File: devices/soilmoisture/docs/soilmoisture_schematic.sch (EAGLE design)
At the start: 31 parts, among them Q1 SSM6P15FU, Q2 SSM6P15FU, Q3 2SK2009, Q4 2SK2009, SW1 OTA_BTN, U1 nRF52832, U2 RFM95C-915, U3 FM25V02-8KB, U4 MCP1700-2502E, U5 W25Q16-2MB

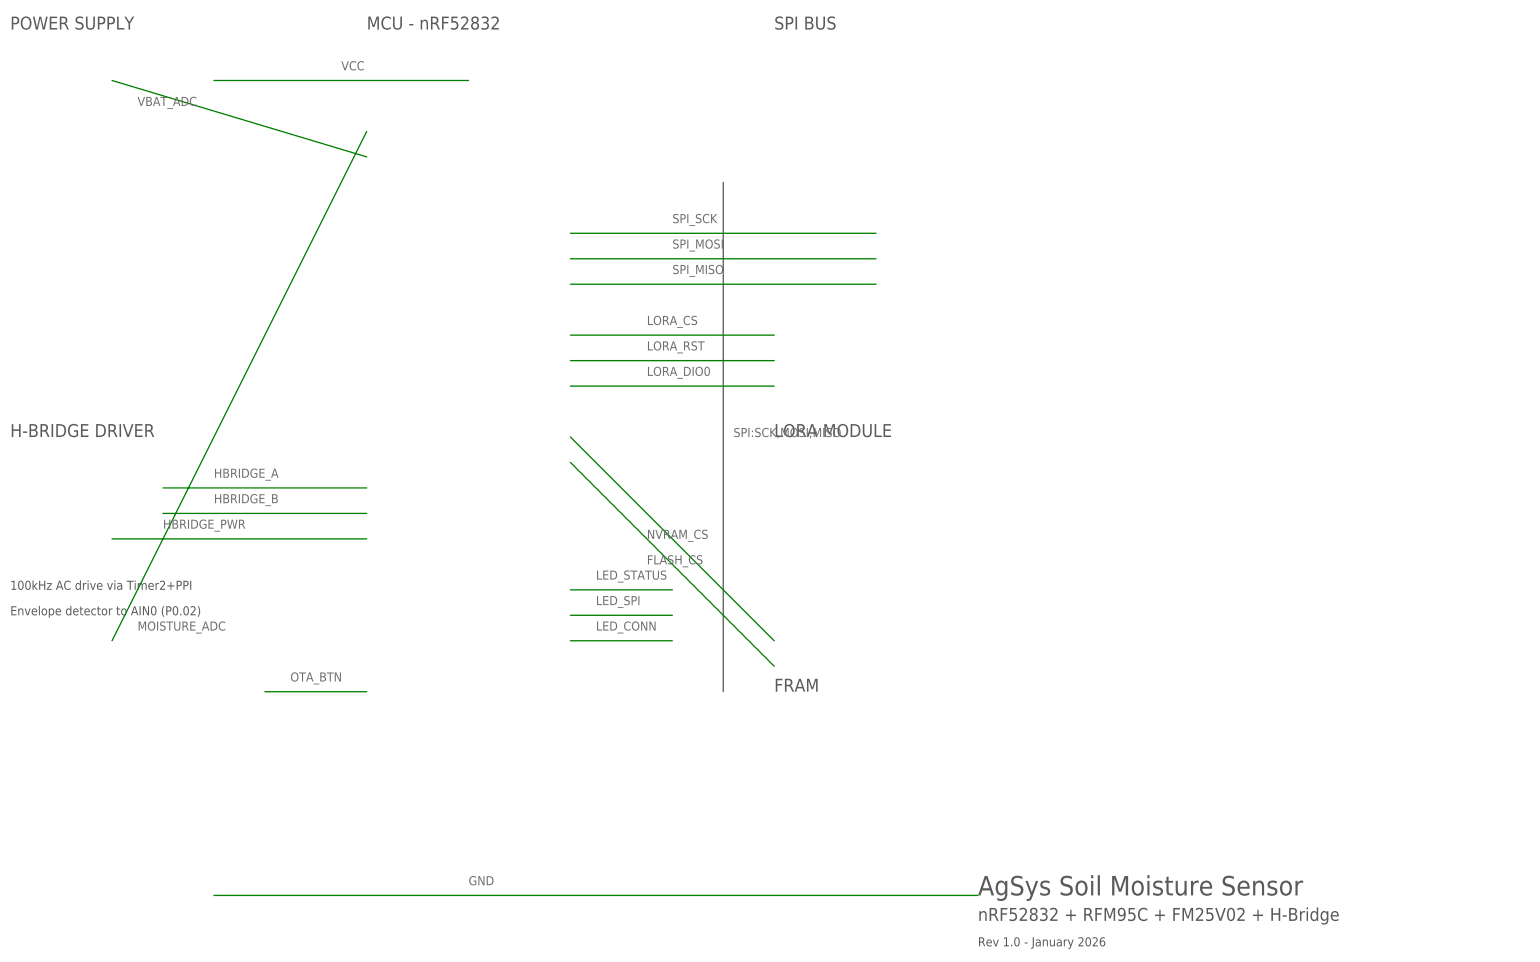
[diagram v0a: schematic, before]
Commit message: Initial commit - the soil moisture controller based on the amazing Nordic Semiconductor vRF52832 micro controller
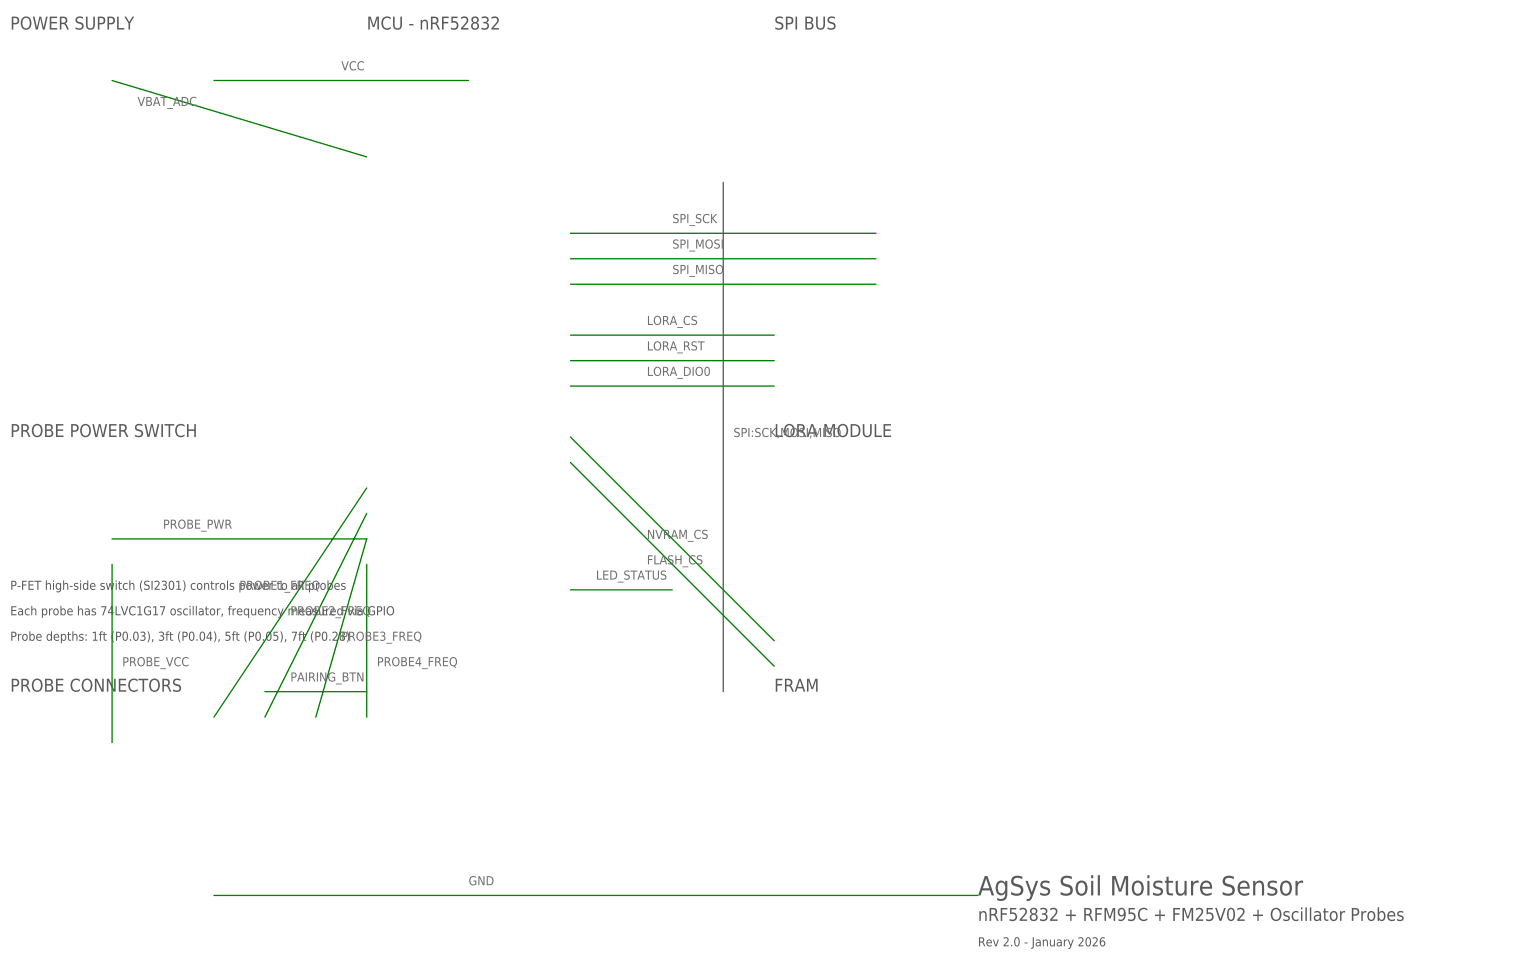
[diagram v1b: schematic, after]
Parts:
- removed D1, D2: BAT54S, diode:BAT54S
- removed LED2: YELLOW, led:LED
- removed LED3: BLUE, led:LED
- removed PROBE1: CAP_PROBE, connector:PROBE
- removed Q2: SSM6P15FU, mosfet:SSM6P15FU
- removed Q3, Q4: 2SK2009, mosfet:2SK2009
- added J1: PROBE1-1FT, connector:CONN_3
- added J2: PROBE2-3FT, connector:CONN_3
- added J3: PROBE3-5FT, connector:CONN_3
- added J4: PROBE4-7FT, connector:CONN_3
- added R7: 10K, resistor:R
- Q1: value SSM6P15FU -> SI2301-PFET; device mosfet:SSM6P15FU -> mosfet:SI2301
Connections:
- net OTA_BTN renamed PAIRING_BTN
- removed net HBRIDGE_A: Q1.G, Q3.G, U1.P0.14
- removed net HBRIDGE_B: Q2.G, Q4.G, U1.P0.15
- removed net HBRIDGE_PWR: U1.P0.16
- removed net LED_CONN: LED3.A, U1.P0.20
- removed net LED_SPI: LED2.A, U1.P0.19
- removed net MOISTURE_ADC: U1.P0.02/AIN0
- new net PROBE1_FREQ: J1.3, U1.P0.03
- new net PROBE2_FREQ: J2.3, U1.P0.04
- new net PROBE3_FREQ: J3.3, U1.P0.05
- new net PROBE4_FREQ: J4.3, U1.P0.28
- new net PROBE_PWR: Q1.G, R7.1, U1.P0.16
- new net PROBE_VCC: J1.1, J2.1, J3.1, J4.1, Q1.S
- net LED_STATUS: now also R3.1
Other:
- note added: "Each probe has 74LVC1G17 oscillator, frequency measured via GPIO"
- note added: "P-FET high-side switch (SI2301) controls power to all probes"
- note added: "PROBE CONNECTORS"
- note added: "PROBE POWER SWITCH"
- note added: "Probe depths: 1ft (P0.03), 3ft (P0.04), 5ft (P0.05), 7ft (P0.28)"
- note added: "Rev 2.0 - January 2026"
- note added: "nRF52832 + RFM95C + FM25V02 + Oscillator Probes"
- note removed: "100kHz AC drive via Timer2+PPI"
- note removed: "Envelope detector to AIN0 (P0.02)"
- note removed: "H-BRIDGE DRIVER"
- note removed: "Rev 1.0 - January 2026"
- note removed: "nRF52832 + RFM95C + FM25V02 + H-Bridge"
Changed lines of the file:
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@@
 <schematic xreflabel="%F%N/%S.%C%R" xrefpart="/%S.%C%R">
 <description>AgSys Soil Moisture Sensor - Wiring Diagram
-nRF52832 + RFM95C LoRa + FM25V02 FRAM + H-Bridge Capacitance Sensor</description>
+nRF52832 + RFM95C LoRa + FM25V02 FRAM + Oscillator Frequency Shift Probes (4x)</description>
 <attributes>
 <attribute name="AUTHOR" value="AgSys Control"/>
-<attribute name="REVISION" value="1.0"/>
+<attribute name="REVISION" value="2.0"/>
 <attribute name="TITLE" value="Soil Moisture Sensor"/>
 </attributes>
@@
 <!-- SPI NOR Flash for firmware backup -->
 <part name="U5" library="flash" deviceset="W25Q16" device="" value="W25Q16-2MB"/>
-<!-- H-Bridge MOSFETs -->
-<part name="Q1" library="mosfet" deviceset="SSM6P15FU" device="" value="SSM6P15FU"/>
-<part name="Q2" library="mosfet" deviceset="SSM6P15FU" device="" value="SSM6P15FU"/>
-<part name="Q3" library="mosfet" deviceset="2SK2009" device="" value="2SK2009"/>
-<part name="Q4" library="mosfet" deviceset="2SK2009" device="" value="2SK2009"/>
-<!-- Flyback Diodes -->
-<part name="D1" library="diode" deviceset="BAT54S" device="" value="BAT54S"/>
-<part name="D2" library="diode" deviceset="BAT54S" device="" value="BAT54S"/>
+<!-- Probe Power Switch (P-FET high-side) -->
+<part name="Q1" library="mosfet" deviceset="SI2301" device="" value="SI2301-PFET"/>
+<!-- Gate pull-up resistor for Q1 -->
+<part name="R7" library="resistor" deviceset="R" device="" value="10K"/>
 <!-- LDO Regulator -->
 <part name="U4" library="regulator" deviceset="MCP1700" device="" value="MCP1700-2502E"/>
 <!-- Battery -->
 <part name="BT1" library="battery" deviceset="21700" device="" value="21700-5000mAh"/>
-<!-- LEDs -->
+<!-- Status LED (single) -->
 <part name="LED1" library="led" deviceset="LED" device="" value="GREEN"/>
-<part name="LED2" library="led" deviceset="LED" device="" value="YELLOW"/>
-<part name="LED3" library="led" deviceset="LED" device="" value="BLUE"/>
 <!-- Resistors -->
 <part name="R1" library="resistor" deviceset="R" device="" value="100K"/>
@@
 <!-- Antenna -->
 <part name="ANT1" library="antenna" deviceset="ANTENNA" device="" value="915MHz"/>
-<!-- Capacitive Probe -->
-<part name="PROBE1" library="connector" deviceset="PROBE" device="" value="CAP_PROBE"/>
+<!-- Oscillator Probe Connectors (4x, 3-pin: VCC, GND, FREQ) -->
+<part name="J1" library="connector" deviceset="CONN_3" device="" value="PROBE1-1FT"/>
+<part name="J2" library="connector" deviceset="CONN_3" device="" value="PROBE2-3FT"/>
+<part name="J3" library="connector" deviceset="CONN_3" device="" value="PROBE3-5FT"/>
+<part name="J4" library="connector" deviceset="CONN_3" device="" value="PROBE4-7FT"/>
 <!-- Power Supply Labels -->
 <part name="VCC" library="supply" deviceset="VCC" device="" value="2.5V"/>
@@
 <!-- Title Block -->
 <text x="200" y="10" size="3.81" layer="97">AgSys Soil Moisture Sensor</text>
-<text x="200" y="5" size="2.54" layer="97">nRF52832 + RFM95C + FM25V02 + H-Bridge</text>
-<text x="200" y="0" size="1.778" layer="97">Rev 1.0 - January 2026</text>
+<text x="200" y="5" size="2.54" layer="97">nRF52832 + RFM95C + FM25V02 + Oscillator Probes</text>
+<text x="200" y="0" size="1.778" layer="97">Rev 2.0 - January 2026</text>
 <!-- Section Labels -->
 <text x="10" y="180" size="2.54" layer="97" font="vector">POWER SUPPLY</text>
 <text x="80" y="180" size="2.54" layer="97" font="vector">MCU - nRF52832</text>
 <text x="160" y="180" size="2.54" layer="97" font="vector">SPI BUS</text>
-<text x="10" y="100" size="2.54" layer="97" font="vector">H-BRIDGE DRIVER</text>
+<text x="10" y="100" size="2.54" layer="97" font="vector">PROBE POWER SWITCH</text>
 <text x="160" y="100" size="2.54" layer="97" font="vector">LORA MODULE</text>
 <text x="160" y="50" size="2.54" layer="97" font="vector">FRAM</text>
+<text x="10" y="50" size="2.54" layer="97" font="vector">PROBE CONNECTORS</text>
 <!-- Connection Notes -->
-<text x="10" y="70" size="1.778" layer="97">100kHz AC drive via Timer2+PPI</text>
-<text x="10" y="65" size="1.778" layer="97">Envelope detector to AIN0 (P0.02)</text>
+<text x="10" y="70" size="1.778" layer="97">P-FET high-side switch (SI2301) controls power to all probes</text>
+<text x="10" y="65" size="1.778" layer="97">Each probe has 74LVC1G17 oscillator, frequency measured via GPIO</text>
+<text x="10" y="60" size="1.778" layer="97">Probe depths: 1ft (P0.03), 3ft (P0.04), 5ft (P0.05), 7ft (P0.28)</text>
 </plain>
 <instances>
@@
 </segment>
 </net>
-<!-- H-Bridge Drive A -->
-<net name="HBRIDGE_A" class="0">
-<segment>
-<pinref part="U1" gate="G$1" pin="P0.14"/>
+<!-- Probe Power Enable (P-FET gate, active LOW) -->
+<net name="PROBE_PWR" class="0">
+<segment>
+<pinref part="U1" gate="G$1" pin="P0.16"/>
 <pinref part="Q1" gate="G$1" pin="G"/>
-<pinref part="Q3" gate="G$1" pin="G"/>
-<wire x1="80" y1="90" x2="40" y2="90" width="0.254" layer="91"/>
-<label x="50" y="92" size="1.778" layer="95"/>
-</segment>
-</net>
-<!-- H-Bridge Drive B -->
-<net name="HBRIDGE_B" class="0">
-<segment>
-<pinref part="U1" gate="G$1" pin="P0.15"/>
-<pinref part="Q2" gate="G$1" pin="G"/>
-<pinref part="Q4" gate="G$1" pin="G"/>
-<wire x1="80" y1="85" x2="40" y2="85" width="0.254" layer="91"/>
-<label x="50" y="87" size="1.778" layer="95"/>
-</segment>
-</net>
-<!-- H-Bridge Power Enable -->
-<net name="HBRIDGE_PWR" class="0">
-<segment>
-<pinref part="U1" gate="G$1" pin="P0.16"/>
+<pinref part="R7" gate="G$1" pin="1"/>
 <wire x1="80" y1="80" x2="30" y2="80" width="0.254" layer="91"/>
 <label x="40" y="82" size="1.778" layer="95"/>
 </segment>
 </net>
-<!-- Moisture ADC -->
-<net name="MOISTURE_ADC" class="0">
-<segment>
-<pinref part="U1" gate="G$1" pin="P0.02/AIN0"/>
-<wire x1="80" y1="160" x2="30" y2="60" width="0.254" layer="91"/>
-<label x="35" y="62" size="1.778" layer="95"/>
+<!-- Probe Power VCC (switched by Q1) -->
+<net name="PROBE_VCC" class="1">
+<segment>
+<pinref part="Q1" gate="G$1" pin="S"/>
+<pinref part="J1" gate="G$1" pin="1"/>
+<pinref part="J2" gate="G$1" pin="1"/>
+<pinref part="J3" gate="G$1" pin="1"/>
+<pinref part="J4" gate="G$1" pin="1"/>
+<wire x1="30" y1="75" x2="30" y2="40" width="0.4064" layer="91"/>
+<label x="32" y="55" size="1.778" layer="95"/>
+</segment>
+</net>
+<!-- Probe 1 Frequency Input (1ft depth) -->
+<net name="PROBE1_FREQ" class="0">
+<segment>
+<pinref part="U1" gate="G$1" pin="P0.03"/>
+<pinref part="J1" gate="G$1" pin="3"/>
+<wire x1="80" y1="90" x2="50" y2="45" width="0.254" layer="91"/>
+<label x="55" y="70" size="1.778" layer="95"/>
+</segment>
+</net>
+<!-- Probe 2 Frequency Input (3ft depth) -->
+<net name="PROBE2_FREQ" class="0">
+<segment>
+<pinref part="U1" gate="G$1" pin="P0.04"/>
+<pinref part="J2" gate="G$1" pin="3"/>
+<wire x1="80" y1="85" x2="60" y2="45" width="0.254" layer="91"/>
+<label x="65" y="65" size="1.778" layer="95"/>
+</segment>
+</net>
+<!-- Probe 3 Frequency Input (5ft depth) -->
+<net name="PROBE3_FREQ" class="0">
+<segment>
+<pinref part="U1" gate="G$1" pin="P0.05"/>
+<pinref part="J3" gate="G$1" pin="3"/>
+<wire x1="80" y1="80" x2="70" y2="45" width="0.254" layer="91"/>
+<label x="75" y="60" size="1.778" layer="95"/>
+</segment>
+</net>
+<!-- Probe 4 Frequency Input (7ft depth) -->
+<net name="PROBE4_FREQ" class="0">
+<segment>
+<pinref part="U1" gate="G$1" pin="P0.28"/>
+<pinref part="J4" gate="G$1" pin="3"/>
+<wire x1="80" y1="75" x2="80" y2="45" width="0.254" layer="91"/>
+<label x="82" y="55" size="1.778" layer="95"/>
 </segment>
 </net>
@@
 </segment>
 </net>
-<!-- LED Status -->
+<!-- Status LED (single green LED for all status indication) -->
 <net name="LED_STATUS" class="0">
 <segment>
 <pinref part="U1" gate="G$1" pin="P0.17"/>
 <pinref part="LED1" gate="G$1" pin="A"/>
+<pinref part="R3" gate="G$1" pin="1"/>
 <wire x1="120" y1="70" x2="140" y2="70" width="0.254" layer="91"/>
 <label x="125" y="72" size="1.778" layer="95"/>
 </segment>
 </net>
-<!-- LED SPI -->
-<net name="LED_SPI" class="0">
-<segment>
-<pinref part="U1" gate="G$1" pin="P0.19"/>
-<pinref part="LED2" gate="G$1" pin="A"/>
-<wire x1="120" y1="65" x2="140" y2="65" width="0.254" layer="91"/>
-<label x="125" y="67" size="1.778" layer="95"/>
-</segment>
-</net>
-<!-- LED BLE -->
-<net name="LED_CONN" class="0">
-<segment>
-<pinref part="U1" gate="G$1" pin="P0.20"/>
-<pinref part="LED3" gate="G$1" pin="A"/>
-<wire x1="120" y1="60" x2="140" y2="60" width="0.254" layer="91"/>
-<label x="125" y="62" size="1.778" layer="95"/>
-</segment>
-</net>
-<!-- OTA Button -->
-<net name="OTA_BTN" class="0">
+<!-- Pairing Button (2s hold to enter BLE pairing mode) -->
+<net name="PAIRING_BTN" class="0">
 <segment>
 <pinref part="U1" gate="G$1" pin="P0.07"/>
